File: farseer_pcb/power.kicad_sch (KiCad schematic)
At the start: 7 parts, among them J1 USB_C_10137062-00021LF, U1 MAX865EUA+

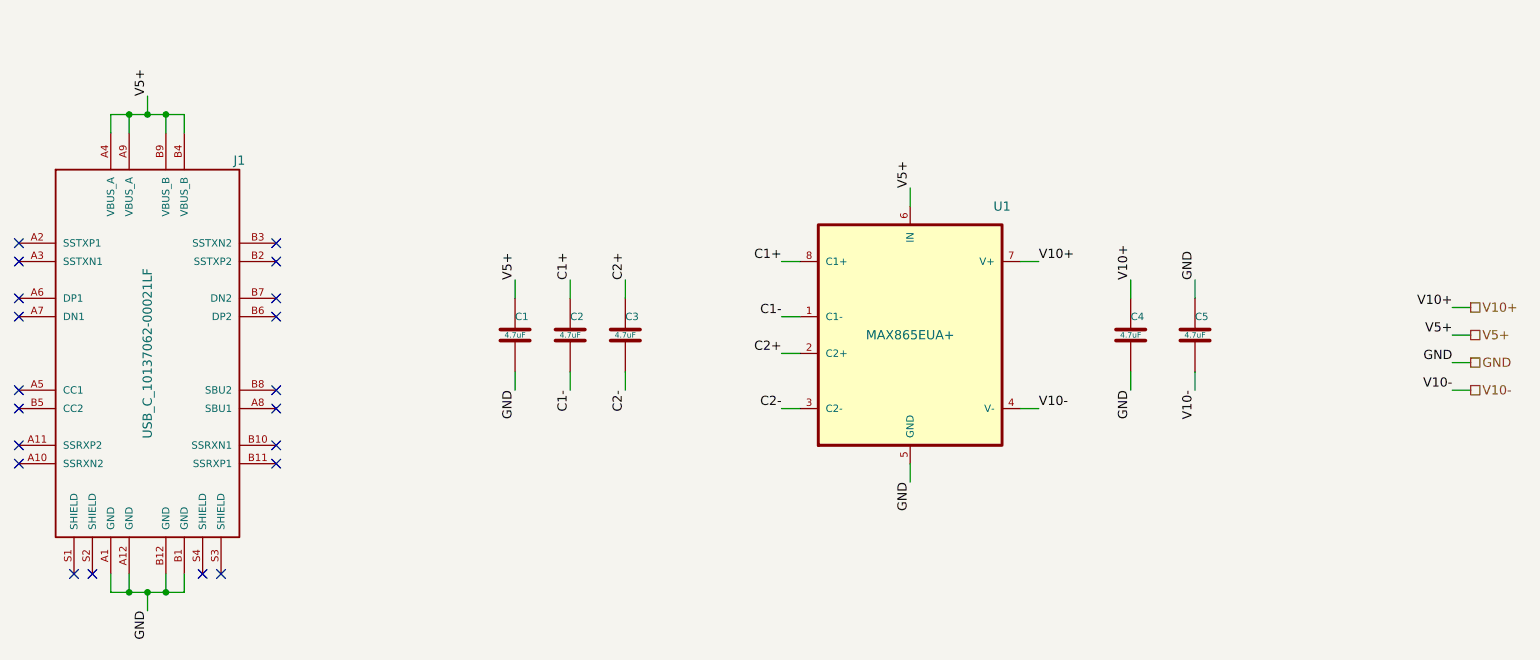
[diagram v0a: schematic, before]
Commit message: Begin board resize
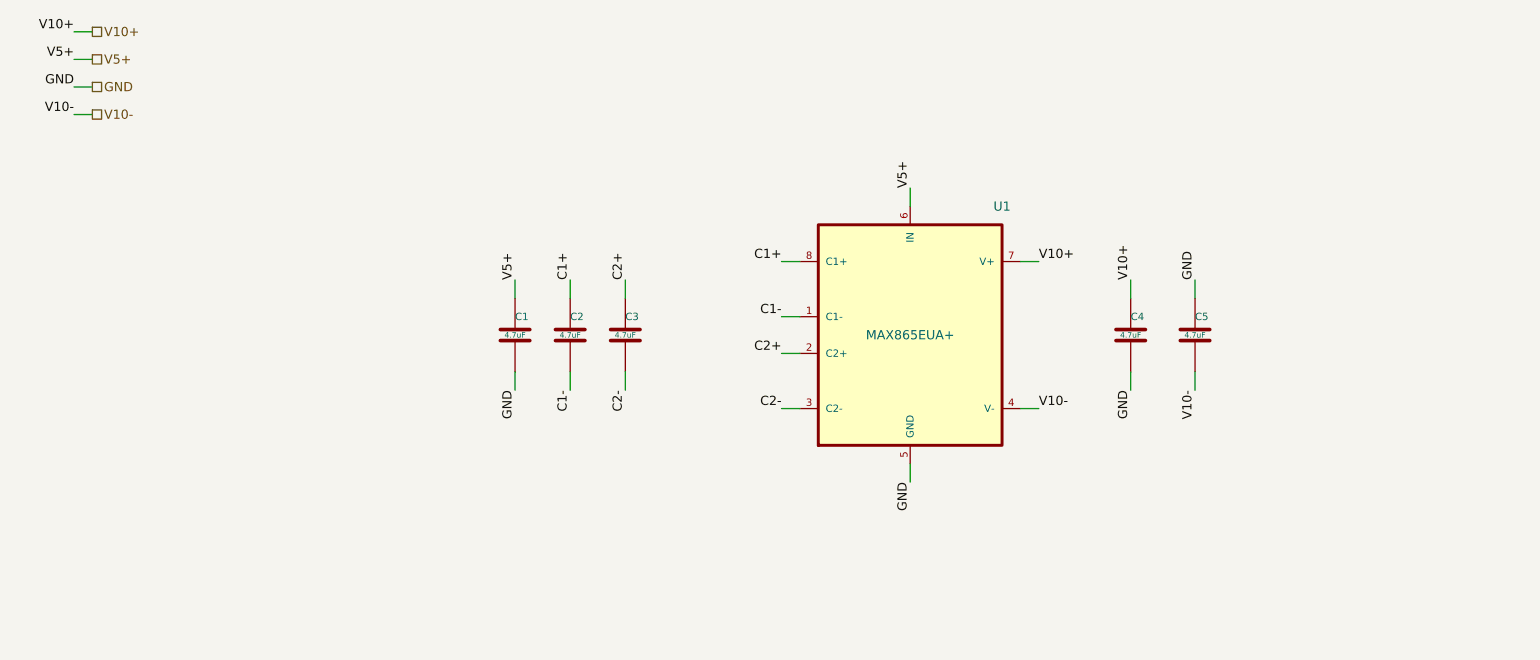
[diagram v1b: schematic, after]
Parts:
- removed J1: USB_C_10137062-00021LF, Janelia:USB_C_Receptacle_Amphenol_10137062-00021LF, symbol Janelia:USB_C_10137062-00021LF
- C1, C2, C3, C4, C5: MFN TDK Corporation -> (none); MPN C1608X5R1C475K080AC -> (none); Manufacturer (none) -> TDK Corporation; Manufacturer Part Number (none) -> C1608X5R1C475K080AC; Synopsis (none) -> CAP CER 4.7UF 16V X5R 0603
- U1: MFN Maxim Integrated -> (none); MPN MAX865EUA+ -> (none); Manufacturer (none) -> Maxim Integrated; Manufacturer Part Number (none) -> MAX865EUA+; Synopsis (none) -> IC REG CHARGE PUMP INV DL 8UMAX
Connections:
- no-connect marks 20 -> 0
